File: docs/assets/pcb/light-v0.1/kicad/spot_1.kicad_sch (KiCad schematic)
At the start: 30 parts, among them U14 spot branch gated eFuse 0.494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, U7 333mA spotlight CC driver, U8 333mA spotlight CC driver, U9 333mA spotlight CC driver

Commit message: Refresh PCB chapters from verified central LED snapshots
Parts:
- C516: Manufacturer (none) -> TDK
- C517, C518, C519, C520, C521, C522: Manufacturer (none) -> Murata
- D501, D502, D503, U7, U8, U9: Manufacturer (none) -> Diodes Incorporated
- L502, L503, L504: Manufacturer (none) -> Bourns
- R515, R516, R517, R518, R519, R520, R521: Manufacturer (none) -> Yageo
- R523, R524, R525: Manufacturer (none) -> Panasonic
- R526, R527, R528: value 10k -> 910; MPN RC0603FR-0710KL -> RC0603FR-07910RL; Manufacturer (none) -> Yageo
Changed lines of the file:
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@@
         (font
           (size 1.0 1.0))))
-    (property "Manufacturer" ""
+    (property "Manufacturer" "Yageo"
       (at 160.02 50.8 0.0)
       (hide yes)
@@
         (font
           (size 1.0 1.0))))
-    (property "Manufacturer" ""
+    (property "Manufacturer" "Yageo"
       (at 215.9 50.8 0.0)
       (hide yes)
@@
         (font
           (size 1.0 1.0))))
-    (property "Manufacturer" ""
+    (property "Manufacturer" "Yageo"
       (at 271.78 50.8 0.0)
       (hide yes)
@@
         (font
           (size 1.0 1.0))))
-    (property "Manufacturer" ""
+    (property "Manufacturer" "Yageo"
       (at 271.78 88.9 0.0)
       (hide yes)
@@
         (font
           (size 1.0 1.0))))
-    (property "Manufacturer" ""
+    (property "Manufacturer" "Yageo"
       (at 160.02 116.84 0.0)
       (hide yes)
@@
         (font
           (size 1.0 1.0))))
-    (property "Manufacturer" ""
+    (property "Manufacturer" "Yageo"
       (at 215.9 116.84 0.0)
       (hide yes)
@@
         (font
           (size 1.0 1.0))))
-    (property "Manufacturer" ""
+    (property "Manufacturer" "Yageo"
       (at 327.66 116.84 0.0)
       (hide yes)
@@
         (font
           (size 1.0 1.0))))
-    (property "Manufacturer" ""
+    (property "Manufacturer" "TDK"
       (at 160.02 83.82 0.0)
       (hide yes)
@@
         (font
           (size 1.0 1.0))))
-    (property "Manufacturer" ""
+    (property "Manufacturer" "Murata"
       (at 27.94 111.76 0.0)
       (hide yes)
@@
         (font
           (size 1.0 1.0))))
-    (property "Manufacturer" ""
+    (property "Manufacturer" "Murata"
       (at 327.66 83.82 0.0)
       (hide yes)
@@
         (font
           (size 1.0 1.0))))
-    (property "Manufacturer" ""
+    (property "Manufacturer" "Diodes Incorporated"
       (at 381.0 83.82 0.0)
       (hide yes)
@@
         (font
           (size 1.0 1.0))))
-    (property "Manufacturer" ""
+    (property "Manufacturer" "Diodes Incorporated"
       (at 43.18 200.66 0.0)
       (hide yes)
@@
         (font
           (size 1.0 1.0))))
-    (property "Manufacturer" ""
+    (property "Manufacturer" "Panasonic"
       (at 83.82 170.18 0.0)
       (hide yes)
@@
           (size 1.0 1.0))
         (justify left)))
-    (property "Value" "10k"
+    (property "Value" "910"
       (at 27.94 231.14 0.0)
       (effects
@@
         (font
           (size 1.0 1.0))))
-    (property "MPN" "RC0603FR-0710KL"
+    (property "MPN" "RC0603FR-07910RL"
       (at 22.86 229.87 0.0)
       (hide yes)
@@
         (font
           (size 1.0 1.0))))
-    (property "Manufacturer" ""
+    (property "Manufacturer" "Yageo"
       (at 22.86 229.87 0.0)
       (hide yes)
@@
         (font
           (size 1.0 1.0))))
-    (property "Datasheet" "https://www.yageogroup.com/component-documentation/download/specsheet/RC0603FR-0710KL"
+    (property "Datasheet" "https://www.yageogroup.com/component-documentation/download/specsheet/RC0603FR-07910RL"
       (at 22.86 229.87 0.0)
       (hide yes)
@@
         (font
           (size 1.0 1.0))))
-    (property "Manufacturer" ""
+    (property "Manufacturer" "Bourns"
       (at 114.3 224.79 0.0)
       (hide yes)
@@
         (font
           (size 1.0 1.0))))
-    (property "Manufacturer" ""
+    (property "Manufacturer" "Diodes Incorporated"
       (at 134.62 199.39 0.0)
       (hide yes)
@@
         (font
           (size 1.0 1.0))))
-    (property "Manufacturer" ""
+    (property "Manufacturer" "Murata"
       (at 22.86 175.26 0.0)
       (hide yes)
@@
         (font
           (size 1.0 1.0))))
-    (property "Manufacturer" ""
+    (property "Manufacturer" "Murata"
       (at 45.72 175.26 0.0)
       (hide yes)
@@
         (font
           (size 1.0 1.0))))
-    (property "Manufacturer" ""
+    (property "Manufacturer" "Diodes Incorporated"
       (at 172.72 200.66 0.0)
       (hide yes)
@@
         (font
           (size 1.0 1.0))))
-    (property "Manufacturer" ""
+    (property "Manufacturer" "Panasonic"
       (at 213.36 170.18 0.0)
       (hide yes)
@@
           (size 1.0 1.0))
         (justify left)))
-    (property "Value" "10k"
+    (property "Value" "910"
       (at 157.48 231.14 0.0)
       (effects
@@
         (font
           (size 1.0 1.0))))
-    (property "MPN" "RC0603FR-0710KL"
+    (property "MPN" "RC0603FR-07910RL"
       (at 152.4 229.87 0.0)
       (hide yes)
@@
         (font
           (size 1.0 1.0))))
-    (property "Manufacturer" ""
+    (property "Manufacturer" "Yageo"
       (at 152.4 229.87 0.0)
       (hide yes)
@@
         (font
           (size 1.0 1.0))))
-    (property "Datasheet" "https://www.yageogroup.com/component-documentation/download/specsheet/RC0603FR-0710KL"
+    (property "Datasheet" "https://www.yageogroup.com/component-documentation/download/specsheet/RC0603FR-07910RL"
       (at 152.4 229.87 0.0)
       (hide yes)
@@
         (font
           (size 1.0 1.0))))
-    (property "Manufacturer" ""
+    (property "Manufacturer" "Bourns"
       (at 243.84 224.79 0.0)
       (hide yes)
@@
         (font
           (size 1.0 1.0))))
-    (property "Manufacturer" ""
+    (property "Manufacturer" "Diodes Incorporated"
       (at 264.16 199.39 0.0)
       (hide yes)
@@
         (font
           (size 1.0 1.0))))
-    (property "Manufacturer" ""
+    (property "Manufacturer" "Murata"
       (at 152.4 175.26 0.0)
       (hide yes)
@@
         (font
           (size 1.0 1.0))))
-    (property "Manufacturer" ""
+    (property "Manufacturer" "Murata"
       (at 175.26 175.26 0.0)
       (hide yes)
@@
         (font
           (size 1.0 1.0))))
-    (property "Manufacturer" ""
+    (property "Manufacturer" "Diodes Incorporated"
       (at 302.26 200.66 0.0)
       (hide yes)
@@
         (font
           (size 1.0 1.0))))
-    (property "Manufacturer" ""
+    (property "Manufacturer" "Panasonic"
       (at 342.9 170.18 0.0)
       (hide yes)
@@
           (size 1.0 1.0))
         (justify left)))
-    (property "Value" "10k"
+    (property "Value" "910"
       (at 287.02 231.14 0.0)
       (effects
@@
         (font
           (size 1.0 1.0))))
-    (property "MPN" "RC0603FR-0710KL"
+    (property "MPN" "RC0603FR-07910RL"
       (at 281.94 229.87 0.0)
       (hide yes)
@@
         (font
           (size 1.0 1.0))))
-    (property "Manufacturer" ""
+    (property "Manufacturer" "Yageo"
       (at 281.94 229.87 0.0)
       (hide yes)
@@
         (font
           (size 1.0 1.0))))
-    (property "Datasheet" "https://www.yageogroup.com/component-documentation/download/specsheet/RC0603FR-0710KL"
+    (property "Datasheet" "https://www.yageogroup.com/component-documentation/download/specsheet/RC0603FR-07910RL"
       (at 281.94 229.87 0.0)
       (hide yes)
@@
         (font
           (size 1.0 1.0))))
-    (property "Manufacturer" ""
+    (property "Manufacturer" "Bourns"
       (at 373.38 224.79 0.0)
       (hide yes)

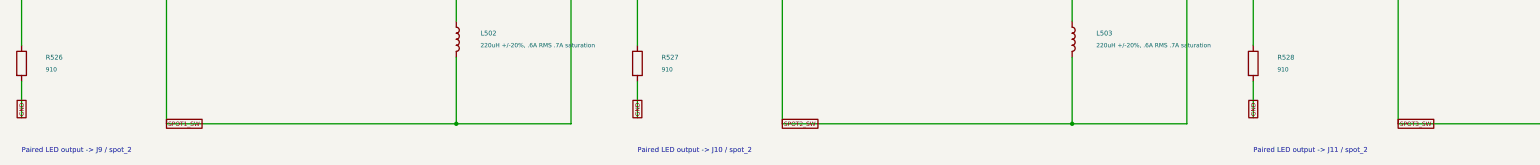
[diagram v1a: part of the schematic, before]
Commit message: Refresh PCB chapters for grouped arm connectors and branded revision
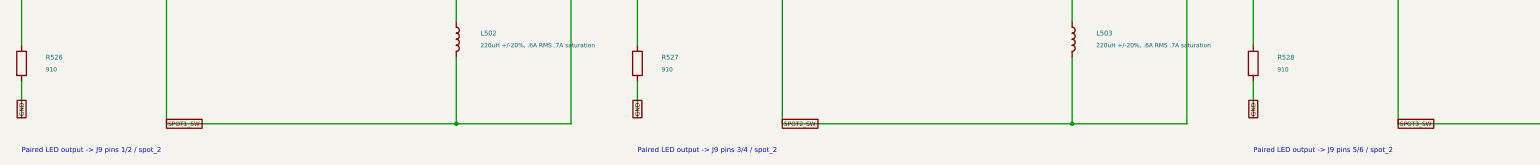
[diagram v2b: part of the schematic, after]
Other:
- note added: "Paired LED output -> J9 pins 1/2 / spot_2"
- note added: "Paired LED output -> J9 pins 3/4 / spot_2"
- note added: "Paired LED output -> J9 pins 5/6 / spot_2"
- note removed: "Paired LED output -> J10 / spot_2"
- note removed: "Paired LED output -> J11 / spot_2"
- note removed: "Paired LED output -> J9 / spot_2"
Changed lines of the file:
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@@
       (justify left top))
 )
-  (text "Paired LED output -> J9 / spot_2"
+  (text "Paired LED output -> J9 pins 1/2 / spot_2"
     (at 22.86 247.65 0)
     (effects
@@
       (justify left top))
 )
-  (text "Paired LED output -> J10 / spot_2"
+  (text "Paired LED output -> J9 pins 3/4 / spot_2"
     (at 152.4 247.65 0)
     (effects
@@
       (justify left top))
 )
-  (text "Paired LED output -> J11 / spot_2"
+  (text "Paired LED output -> J9 pins 5/6 / spot_2"
     (at 281.94 247.65 0)
     (effects
